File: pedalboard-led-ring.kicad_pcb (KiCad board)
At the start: 2 copper layers, 36 x 28 mm, 16 parts, among them J1 Conn_02x03, U1 TLC5973, U2 LT3494AEDDBPBF

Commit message: Add Versioning information
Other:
- board text added: "${TITLE} ${COMPANY} BCB: ${REVISION}"
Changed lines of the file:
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@@
   )
   (paper "A4")
+  (title_block
+    (title "Pedalboard LED Ring")
+    (date "2023-05-29")
+    (rev "1.0.0")
+    (company "https://github.com/pedalboard")
+    (comment 1 "Source Code: https://github.com/pedalboard/pedalboard-led-ring")
+    (comment 2 "License: CERN Open Hardware Licence Version 2 - Permissive")
+  )
   (layers
     (0 "F.Cu" signal)
@@
     (property "ki_keywords" "LED current driver 12bit PWM")
     (attr smd)
-    (fp_text reference "U1" (at -2.8 -3.5) (layer "B.SilkS")
+    (fp_text reference "U1" (at -4.9 2.2) (layer "B.SilkS")
         (effects (font (size 1 1) (thickness 0.15)) (justify mirror))
     )
@@
   (gr_arc (start 101 46) (mid 101.707107 46.292893) (end 102 47)
     (stroke (width 0.1) (type default)) (layer "Edge.Cuts"))
+  (gr_text "${TITLE}\n${COMPANY}\nBCB: ${REVISION}" (at 66.5 51) (layer "B.SilkS")
+    (effects (font (size 1 1) (thickness 0.15)) (justify right bottom mirror))
+  )
   (dimension (type aligned) (layer "Dwgs.User")
     (pts (xy 66 47.5) (xy 102 47.5))

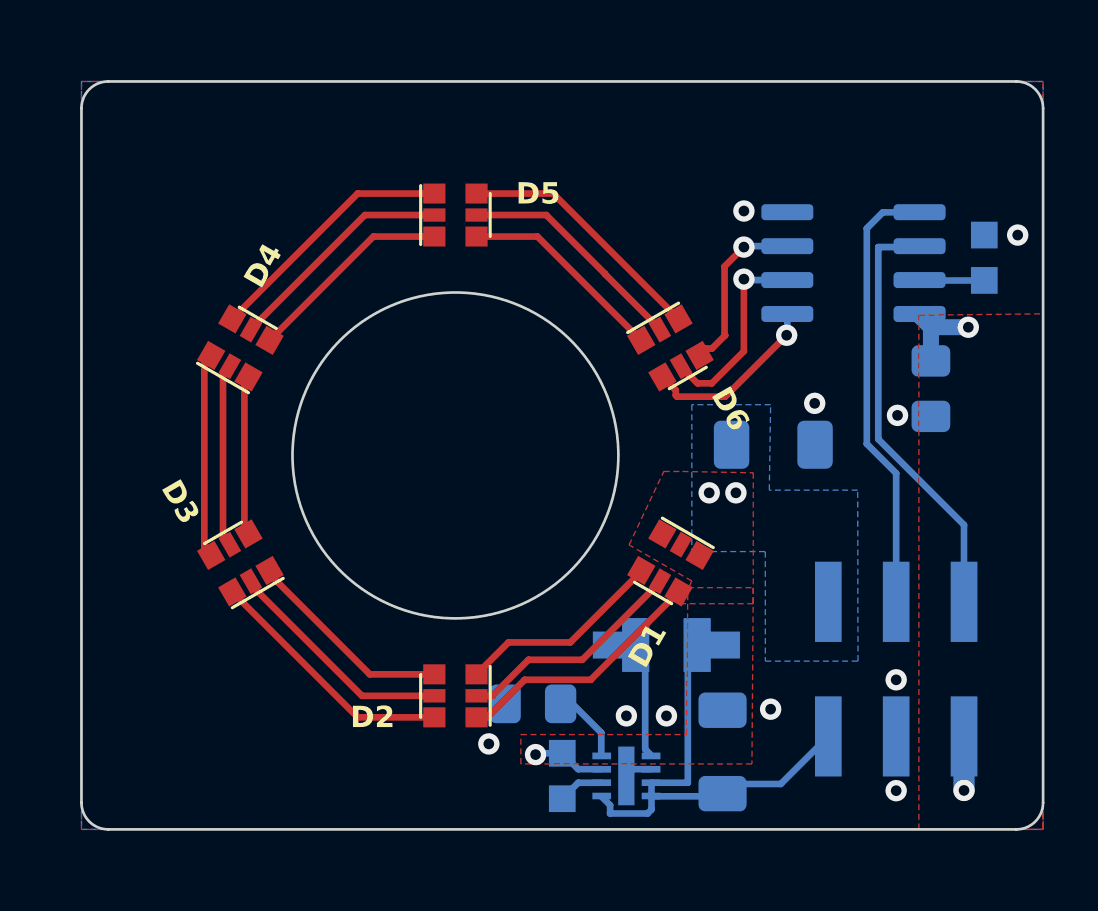
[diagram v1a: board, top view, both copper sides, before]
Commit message: Update design to use neopixel
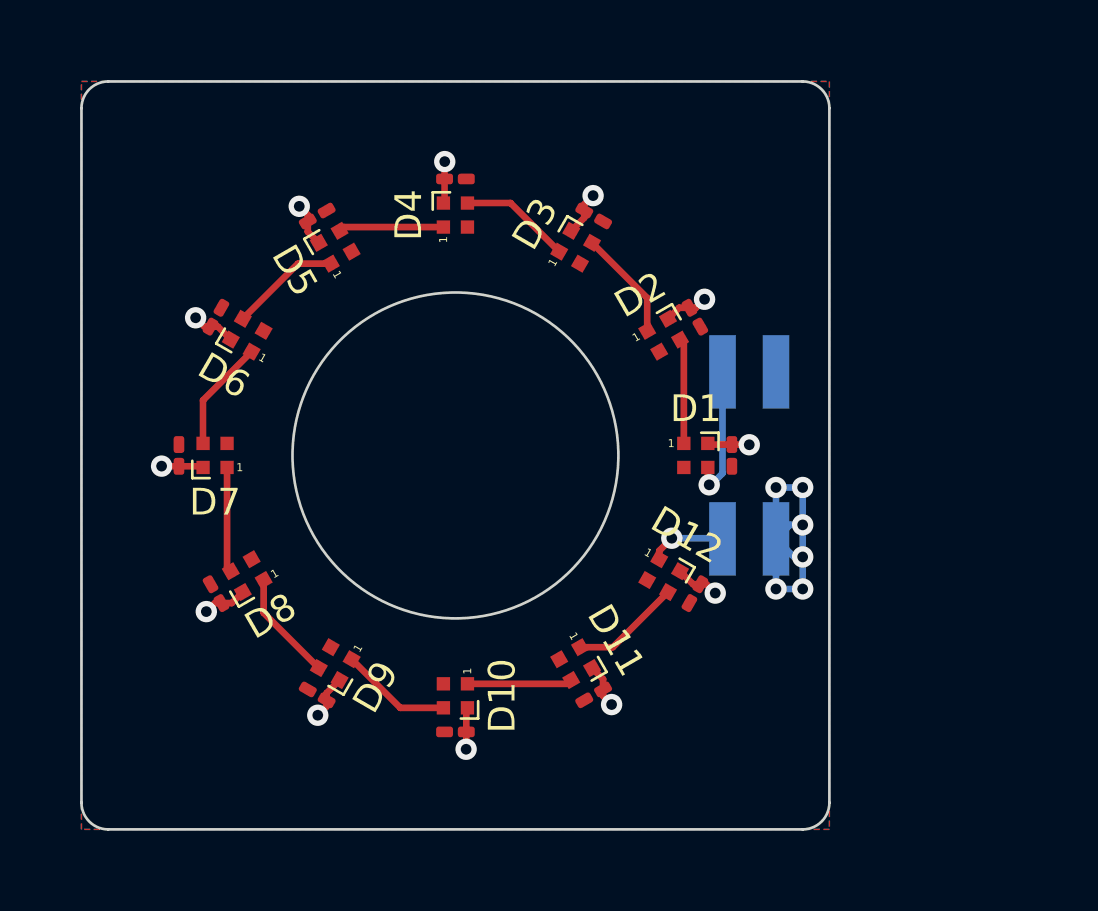
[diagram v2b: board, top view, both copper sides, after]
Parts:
- removed L1: 10uH, Library:IND_LQH32CN150K53L
- removed R1: 5K1, PCM_4ms_Resistor:R_0603
- removed R2: 3.4M, PCM_4ms_Resistor:R_0603
- removed U1: TLC5973, Package_SO:SOIC-8_3.9x4.9mm_P1.27mm
- removed U2: LT3494AEDDBPBF, Package_DFN_QFN:DFN-8-1EP_2x3mm_P0.5mm_EP0.61x2.2mm
- added C10: 1uF, Capacitor_SMD:C_0201_0603Metric_Pad0.64x0.40mm_HandSolder, F.Cu at (80.0, 70.3)
- added C11: 1uF, Capacitor_SMD:C_0201_0603Metric_Pad0.64x0.40mm_HandSolder, F.Cu at (85.2, 69.0)
- added C12: 1uF, Capacitor_SMD:C_0201_0603Metric_Pad0.64x0.40mm_HandSolder, F.Cu at (89.0, 65.2)
- added C5: 1uF, Capacitor_SMD:C_0201_0603Metric_Pad0.64x0.40mm_HandSolder, F.Cu at (74.8, 51.0)
- added C6: 1uF, Capacitor_SMD:C_0201_0603Metric_Pad0.64x0.40mm_HandSolder, F.Cu at (71.0, 54.8)
- added C7: 1uF, Capacitor_SMD:C_0201_0603Metric_Pad0.64x0.40mm_HandSolder, F.Cu at (69.7, 60.0)
- added C8: 1uF, Capacitor_SMD:C_0201_0603Metric_Pad0.64x0.40mm_HandSolder, F.Cu at (71.0, 65.2)
- added C9: 1uF, Capacitor_SMD:C_0201_0603Metric_Pad0.64x0.40mm_HandSolder, F.Cu at (74.8, 69.0)
- added D10: SK6812MINI, LED_SMD:LED_SK6812_EC15_1.5x1.5mm, F.Cu at (80.0, 69.0)
- added D11: SK6812MINI, LED_SMD:LED_SK6812_EC15_1.5x1.5mm, F.Cu at (84.5, 67.8)
- added D12: SK6812MINI, LED_SMD:LED_SK6812_EC15_1.5x1.5mm, F.Cu at (87.8, 64.5)
- added D7: SK6812MINI, LED_SMD:LED_SK6812_EC15_1.5x1.5mm, F.Cu at (71.0, 60.0)
- added D8: SK6812MINI, LED_SMD:LED_SK6812_EC15_1.5x1.5mm, F.Cu at (72.2, 64.5)
- added D9: SK6812MINI, LED_SMD:LED_SK6812_EC15_1.5x1.5mm, F.Cu at (75.5, 67.8)
- C1: value 2.2uF_0603_25V -> 1uF; footprint Capacitor_SMD:C_1206_3216Metric_Pad1.33x1.80mm_HandSolder -> Capacitor_SMD:C_0201_0603Metric_Pad0.64x0.40mm_HandSolder; moved to F.Cu
- C2, C4: value 330nF -> 1uF; footprint Capacitor_SMD:C_0805_2012Metric_Pad1.18x1.45mm_HandSolder -> Capacitor_SMD:C_0201_0603Metric_Pad0.64x0.40mm_HandSolder; moved to F.Cu
- C3: value 10uF_0805_25V -> 1uF; footprint Capacitor_SMD:C_1206_3216Metric_Pad1.33x1.80mm_HandSolder -> Capacitor_SMD:C_0201_0603Metric_Pad0.64x0.40mm_HandSolder; moved to F.Cu
- D1, D2, D3, D4, D5, D6: value RGB-LED -> SK6812MINI; footprint Library:LED_RGB -> LED_SMD:LED_SK6812_EC15_1.5x1.5mm
- J1: value Conn_02x03 -> Conn_02x02_Odd_Even; footprint Connector_PinSocket_2.54mm:PinSocket_2x03_P2.54mm_Vertical_SMD -> Connector_PinSocket_2.00mm:PinSocket_2x02_P2.00mm_Vertical_SMD
- moved C3 20.6 mm to (85.2, 51.0), turned to -30 degrees
- moved C4 19.9 mm to (80.0, 49.6), turned to 0 degrees
- moved D3 17.2 mm to (84.5, 52.2), turned to 60 degrees
- moved D6 15.9 mm to (72.2, 55.5), turned to 150 degrees
- moved D2 15.6 mm to (87.8, 55.5), turned to 30 degrees
- moved J1 9.71 mm to (91.0, 60.0), turned to 90 degrees
- moved D4 9.46 mm to (80.0, 51.0), turned to 90 degrees
- moved C2 9.23 mm to (89.0, 54.8), turned to -60 degrees
- moved D5 4.66 mm to (75.5, 52.2), turned to 120 degrees
- moved D1 4.14 mm to (89.0, 60.0), turned to 0 degrees
- moved C1 1.60 mm to (90.3, 60.0), turned to -90 degrees
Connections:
- C1 pad 1: VDC -> VCC
- C3 pad 1: Net-(J1-SDO) -> VCC
- C4 pad 1: Net-(U2-CAP) -> VCC
- D1 pad 1: VDC -> Net-(D1-DOUT)
- D1 pad 2: VDC -> GND
- D1 pad 3: VDC -> Net-(D1-DIN)
- D1 pad 4: Net-(D1-KB) -> VCC
- D2 pad 1: Net-(D1-KG) -> Net-(D2-DOUT)
- D2 pad 2: Net-(D1-KR) -> GND
- D2 pad 3: Net-(D1-KB) -> Net-(D1-DOUT)
- D2 pad 4: Net-(D2-KB) -> VCC
- D3 pad 1: Net-(D2-KG) -> Net-(D3-DOUT)
- D3 pad 2: Net-(D2-KR) -> GND
- D3 pad 3: Net-(D2-KB) -> Net-(D2-DOUT)
- D3 pad 4: Net-(D3-KB) -> VCC
- D4 pad 1: Net-(D3-KG) -> Net-(D4-DOUT)
- D4 pad 2: Net-(D3-KR) -> GND
- D4 pad 3: Net-(D3-KB) -> Net-(D3-DOUT)
- D4 pad 4: Net-(D4-KB) -> VCC
- D5 pad 1: Net-(D4-KG) -> Net-(D5-DOUT)
- D5 pad 2: Net-(D4-KR) -> GND
- D5 pad 3: Net-(D4-KB) -> Net-(D4-DOUT)
- D5 pad 4: Net-(D5-KB) -> VCC
- D6 pad 1: Net-(D5-KG) -> Net-(D6-DOUT)
- D6 pad 2: Net-(D5-KR) -> GND
- D6 pad 3: Net-(D5-KB) -> Net-(D5-DOUT)
- D6 pad 4: Net-(D6-KB) -> VCC
- J1 pad 1: Net-(J1-SDO) -> VCC
- J1 pad 2: VDC -> GND
- J1 pad 3: GND -> Net-(D1-DIN)
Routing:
- net Net-(J1-SDO): track 17.2 -> 0.00 mm
- net Net-(U1-SDI): track 16.2 -> 0.00 mm
- net VCC: track 5.36 -> 19.3 mm, vias 2 -> 12
- net Net-(D12-DOUT): track 16.7 -> 2.86 mm, vias 0 -> 1
- net GND: track 1.05 -> 12.1 mm, vias 10 -> 6
- net Net-(D2-KG): track 9.51 -> 0.00 mm
- net Net-(D1-KG): track 9.51 -> 0.00 mm
- net Net-(D5-KG): track 9.51 -> 0.00 mm
- net Net-(D4-KG): track 9.51 -> 0.00 mm
- net Net-(D2-KR): track 8.72 -> 0.00 mm
- net Net-(D1-KR): track 8.66 -> 0.00 mm
- net Net-(D5-KR): track 8.66 -> 0.00 mm
- net Net-(D4-KR): track 8.65 -> 0.00 mm
- net Net-(D2-KB): track 7.86 -> 0.00 mm
- net Net-(D1-KB): track 7.80 -> 0.00 mm
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- added copper zone on B.Cu, net VCC
- removed copper zone on B.Cu, net GND
- removed copper zone on F.Cu, net VCC
- removed copper zone on B.Cu, net VDC
- removed copper zone on F.Cu, net VDC
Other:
- board size 36 x 28 mm -> 28 x 28 mm

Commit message: Improve description on silkscreen
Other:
- board text added: "${TITLE} ${COMPANY}"
- board text added: "PCB: ${REVISION}"
- board text removed: "${TITLE} ${COMPANY} BCB: ${REVISION}"
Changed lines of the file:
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@@
   (paper "A4")
   (title_block
-    (title "Pedalboard neopixel Ring")
+    (title "Pedalboard LED Ring")
     (date "2023-05-29")
     (rev "1.0.0")
@@
   (gr_arc (start 93 46) (mid 93.707107 46.292893) (end 94 47)
     (stroke (width 0.1) (type default)) (layer "Edge.Cuts"))
-  (gr_text "${TITLE}\n${COMPANY}\nBCB: ${REVISION}" (at 66.5 51) (layer "B.SilkS")
-    (effects (font (size 1 1) (thickness 0.15)) (justify right bottom mirror))
+  (gr_text "PCB: ${REVISION}" (at 80 73.4) (layer "B.SilkS")
+    (effects (font (size 0.5 0.5) (thickness 0.125)) (justify bottom mirror))
+  )
+  (gr_text "${TITLE}\n${COMPANY}" (at 79.8 48.4) (layer "B.SilkS")
+    (effects (font (size 0.75 0.75) (thickness 0.15)) (justify bottom mirror))
   )
   (dimension (type aligned) (layer "Dwgs.User")

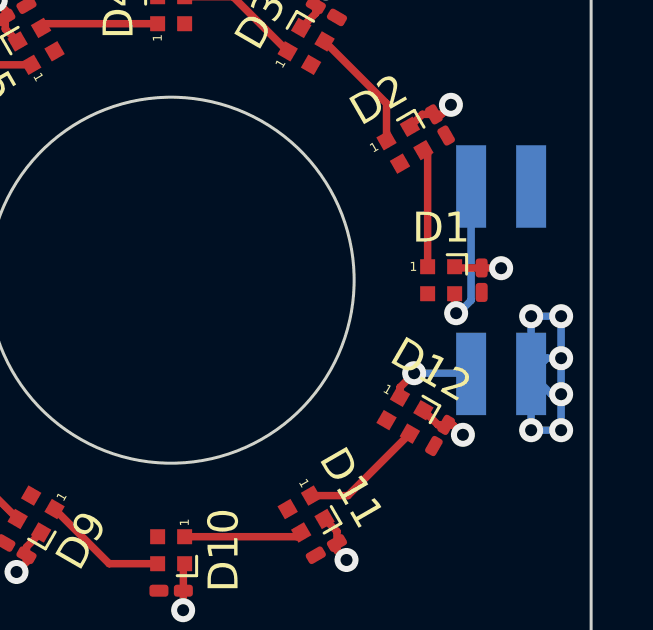
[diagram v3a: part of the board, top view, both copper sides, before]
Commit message: Add an input resistor as recommended by Adafruit's neopixel uberguide
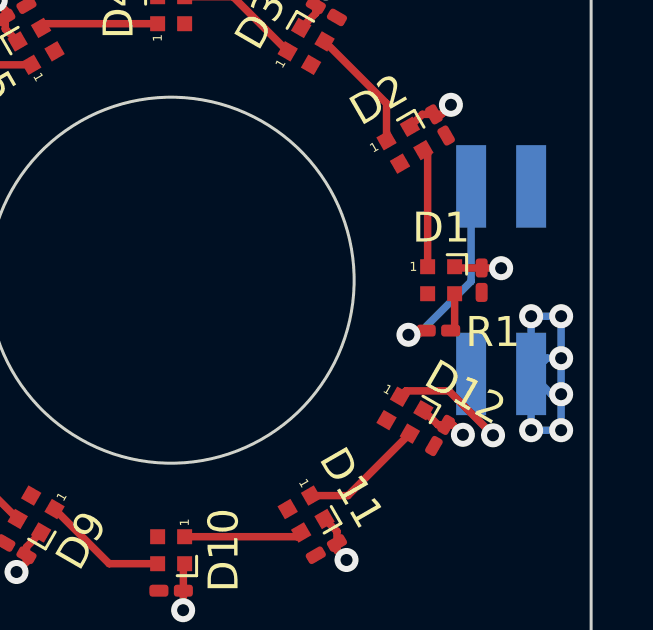
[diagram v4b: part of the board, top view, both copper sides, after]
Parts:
- added R1: 330, Resistor_SMD:R_0201_0603Metric_Pad0.64x0.40mm_HandSolder, F.Cu at (88.9, 61.7)
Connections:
- J1 pad 3: Net-(D1-DIN) -> Net-(J1-Pin_3)
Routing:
- net Net-(J1-Pin_3): track 0.00 -> 6.50 mm, vias 0 -> 1
- net Net-(D1-DIN): track 5.17 -> 1.28 mm, vias 1 -> 0
- net Net-(D12-DOUT): track 2.86 -> 6.18 mm
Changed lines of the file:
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@@
   (net 14 "Net-(D11-DOUT)")
   (net 15 "Net-(D10-DOUT)")
+  (net 16 "Net-(J1-Pin_3)")
   (footprint "Capacitor_SMD:C_0201_0603Metric_Pad0.64x0.40mm_HandSolder" (layer "F.Cu")
     (at 71.036637 65.175 120)
@@
     (property "ki_keywords" "RGB LED NeoPixel Mini addressable")
     (attr smd)
-    (fp_text reference "D12" (at 0 -1.75 150) (layer "F.SilkS")
+    (fp_text reference "D12" (at 1.365709 -1.666065 150) (layer "F.SilkS")
         (effects (font (size 1 1) (thickness 0.15)))
     )
@@
       (net 9 "VCC") (pinfunction "VDD") (pintype "power_in"))
     (model "${KICAD6_3DMODEL_DIR}/LED_SMD.3dshapes/LED_SK6812_EC15_1.5x1.5mm.wrl"
+      (offset (xyz 0 0 0))
+      (scale (xyz 1 1 1))
+      (rotate (xyz 0 0 0))
+    )
+  )
+  (footprint "Resistor_SMD:R_0201_0603Metric_Pad0.64x0.40mm_HandSolder" (layer "F.Cu")
+    (at 88.91 61.68 180)
+    (descr "Resistor SMD 0201 (0603 Metric), square (rectangular) end terminal, IPC_7351 nominal with elongated pad for handsoldering. (Body size source: https://www.vishay.com/docs/20052/crcw0201e3.pdf), generated with kicad-footprint-generator")
+    (tags "resistor handsolder")
+    (property "Sheetfile" "pedalboard-led-ring.kicad_sch")
+    (property "Sheetname" "")
+    (property "ki_description" "Resistor")
+    (property "ki_keywords" "R res resistor")
+    (attr smd)
+    (fp_text reference "R1" (at -1.81 -0.05) (layer "F.SilkS")
+        (effects (font (size 1 1) (thickness 0.15)))
+    )
+    (fp_text value "330" (at 0 1.05) (layer "F.Fab")
+        (effects (font (size 1 1) (thickness 0.15)))
+    )
+    (fp_text user "${REFERENCE}" (at 0 -0.68) (layer "F.Fab")
+        (effects (font (size 0.25 0.25) (thickness 0.04)))
+    )
+    (fp_line (start -0.88 -0.35) (end 0.88 -0.35)
+      (stroke (width 0.05) (type solid)) (layer "F.CrtYd"))
+    (fp_line (start -0.88 0.35) (end -0.88 -0.35)
+      (stroke (width 0.05) (type solid)) (layer "F.CrtYd"))
+    (fp_line (start 0.88 -0.35) (end 0.88 0.35)
+      (stroke (width 0.05) (type solid)) (layer "F.CrtYd"))
+    (fp_line (start 0.88 0.35) (end -0.88 0.35)
+      (stroke (width 0.05) (type solid)) (layer "F.CrtYd"))
+    (fp_line (start -0.3 -0.15) (end 0.3 -0.15)
+      (stroke (width 0.1) (type solid)) (layer "F.Fab"))
+    (fp_line (start -0.3 0.15) (end -0.3 -0.15)
+      (stroke (width 0.1) (type solid)) (layer "F.Fab"))
+    (fp_line (start 0.3 -0.15) (end 0.3 0.15)
+      (stroke (width 0.1) (type solid)) (layer "F.Fab"))
+    (fp_line (start 0.3 0.15) (end -0.3 0.15)
+      (stroke (width 0.1) (type solid)) (layer "F.Fab"))
+    (pad "" smd roundrect (at -0.4325 0 180) (size 0.458 0.36) (layers "F.Paste") (roundrect_rratio 0.25))
+    (pad "" smd roundrect (at 0.4325 0 180) (size 0.458 0.36) (layers "F.Paste") (roundrect_rratio 0.25))
+    (pad "1" smd roundrect (at -0.4075 0 180) (size 0.635 0.4) (layers "F.Cu" "F.Mask") (roundrect_rratio 0.25)
+      (net 2 "Net-(D1-DIN)") (pintype "passive"))
+    (pad "2" smd roundrect (at 0.4075 0 180) (size 0.635 0.4) (layers "F.Cu" "F.Mask") (roundrect_rratio 0.25)
+      (net 16 "Net-(J1-Pin_3)") (pintype "passive"))
+    (model "${KICAD6_3DMODEL_DIR}/Resistor_SMD.3dshapes/R_0201_0603Metric.wrl"
       (offset (xyz 0 0 0))
       (scale (xyz 1 1 1))
@@
       (net 10 "GND") (pinfunction "Pin_2") (pintype "passive"))
     (pad "3" smd rect (at 3.125 -1 90) (size 2.75 1) (layers "B.Cu" "B.Paste" "B.Mask")
-      (net 2 "Net-(D1-DIN)") (pinfunction "Pin_3") (pintype "passive"))
+      (net 16 "Net-(J1-Pin_3)") (pinfunction "Pin_3") (pintype "passive"))
     (pad "4" smd rect (at -3.125 -1 90) (size 2.75 1) (layers "B.Cu" "B.Paste" "B.Mask")
       (net 8 "Net-(D12-DOUT)") (pinfunction "Pin_4") (pintype "passive"))
@@
   (segment (start 88.55 59.55) (end 88.55 55.805771) (width 0.25) (layer "F.Cu") (net 1))
   (segment (start 88.55 55.805771) (end 88.40894 55.664711) (width 0.25) (layer "F.Cu") (net 1))
-  (segment (start 89.45 60.45) (end 89.45 61.120498) (width 0.25) (layer "F.Cu") (net 2))
-  (via (at 89.5 61.1) (size 0.8) (drill 0.4) (layers "F.Cu" "B.Cu") (net 2))
-  (segment (start 90 60.670498) (end 90 56.875) (width 0.25) (layer "B.Cu") (net 2))
-  (segment (start 89.5 61.170498) (end 90 60.670498) (width 0.25) (layer "B.Cu") (net 2))
+  (segment (start 89.45 60.45) (end 89.45 61.5475) (width 0.25) (layer "F.Cu") (net 2))
+  (segment (start 89.45 61.5475) (end 89.3175 61.68) (width 0.25) (layer "F.Cu") (net 2))
   (segment (start 87.179518 55.335289) (end 87.179518 54.105867) (width 0.25) (layer "F.Cu") (net 3))
   (segment (start 87.179518 54.105867) (end 85.114711 52.04106) (width 0.25) (layer "F.Cu") (net 3))
@@
   (segment (start 70.55 57.935193) (end 70.55 59.55) (width 0.25) (layer "F.Cu") (net 7))
   (segment (start 72.370482 56.114711) (end 70.55 57.935193) (width 0.25) (layer "F.Cu") (net 7))
-  (segment (start 87.629518 63.885289) (end 87.629518 63.570482) (width 0.25) (layer "F.Cu") (net 8))
-  (segment (start 87.629518 63.570482) (end 88.1 63.1) (width 0.25) (layer "F.Cu") (net 8))
-  (via (at 88.1 63.1) (size 0.8) (drill 0.4) (layers "F.Cu" "B.Cu") (net 8))
-  (segment (start 88.1 63.1) (end 89.975 63.1) (width 0.25) (layer "B.Cu") (net 8))
+  (segment (start 87.826024 63.688783) (end 89.258493 63.688783) (width 0.25) (layer "F.Cu") (net 8))
+  (segment (start 89.258493 63.688783) (end 90.704826 65.135116) (width 0.25) (layer "F.Cu") (net 8))
+  (segment (start 87.629518 63.885289) (end 87.826024 63.688783) (width 0.25) (layer "F.Cu") (net 8))
+  (segment (start 90.704826 65.135116) (end 90.704826 65.196844) (width 0.25) (layer "F.Cu") (net 8))
+  (via (at 90.73 65.17) (size 0.8) (drill 0.4) (layers "F.Cu" "B.Cu") (net 8))
+  (segment (start 90.704826 65.196844) (end 90.704826 65.135116) (width 0.25) (layer "B.Cu") (net 8))
+  (segment (start 90.704826 65.135116) (end 90 64.43029) (width 0.25) (layer "B.Cu") (net 8))
+  (segment (start 90 64.43029) (end 90 63.125) (width 0.25) (layer "B.Cu") (net 8))
   (segment (start 90.35 59.5925) (end 90.9925 59.5925) (width 0.25) (layer "F.Cu") (net 9))
   (segment (start 70.832887 55.177905) (end 70.605216 55.177905) (width 0.25) (layer "F.Cu") (net 9))
@@
   (segment (start 84.194229 68.55) (end 84.335289 68.40894) (width 0.25) (layer "F.Cu") (net 15))
   (segment (start 80.45 68.55) (end 84.194229 68.55) (width 0.25) (layer "F.Cu") (net 15))
+  (segment (start 88.36 61.68) (end 88.05 61.99) (width 0.25) (layer "F.Cu") (net 16))
+  (segment (start 88.5025 61.68) (end 88.36 61.68) (width 0.25) (layer "F.Cu") (net 16))
+  (via (at 87.91 61.82) (size 0.8) (drill 0.4) (layers "F.Cu" "B.Cu") (net 16))
+  (segment (start 90 60.04) (end 90 56.875) (width 0.25) (layer "B.Cu") (net 16))
+  (segment (start 88.05 61.99) (end 90 60.04) (width 0.25) (layer "B.Cu") (net 16))
   (zone (net 10) (net_name "GND") (layer "F.Cu") (hatch edge 0.5)
     (connect_pads (clearance 0.2))
